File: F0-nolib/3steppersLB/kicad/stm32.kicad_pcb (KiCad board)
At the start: 2 copper layers, 97 x 69.5 mm, 103 parts, among them J1 01x03, J10 Screw_Terminal_01x03, J11 USB_B, J12 Screw_Terminal_01x02, J13 Screw_Terminal_01x02, J14 Conn_01x04_Female, J15 Conn_01x04_Female, J16 Conn_01x04_Female, J17 Conn_01x04_Female, J18 buzzer, J2 Conn_01x04_Female, J3 Conn_01x04_Female, J4 Conn_01x04_Female, J5 Conn_01x04_Female, J6 01x03, J7 Screw_Terminal_01x03, J8 01x05, J9 01x05, K1 G5LE-1, P1 Hole, P2 Hole, P6 Hole, P7 Hole, Q1 B0505S, Q2 SI2300, Q3 SI2300, Q4 SI2300, Q5 IRF9310, SW1 SW_DIP_x01, U1 ISO1050DUB, U2 STM32F072C8Tx, U3 LM2576-5.0, U4 CD4050, U5 CD4050, U6 LM1117-3.3

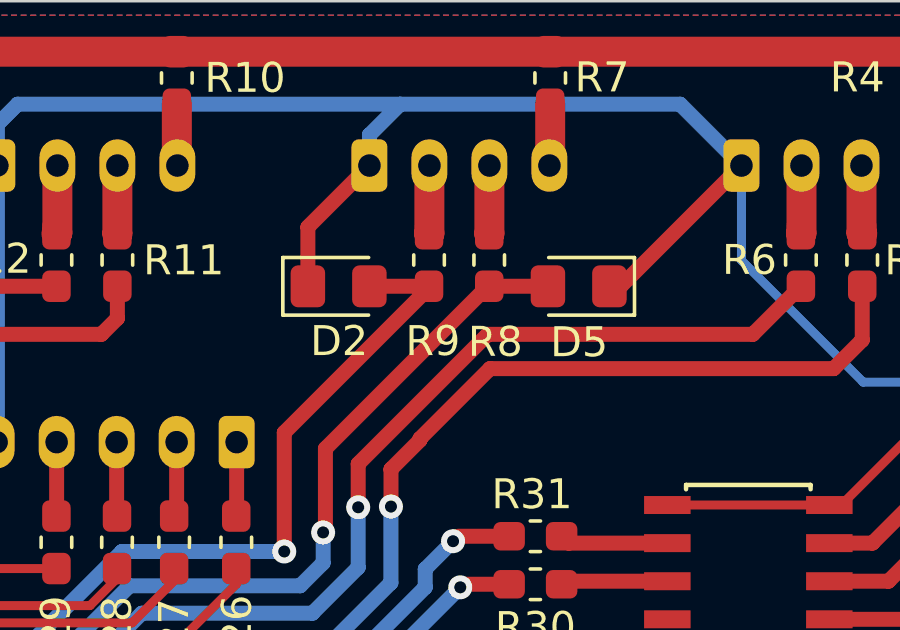
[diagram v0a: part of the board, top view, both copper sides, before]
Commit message: fixed some bugs in 3steppersLB schematic
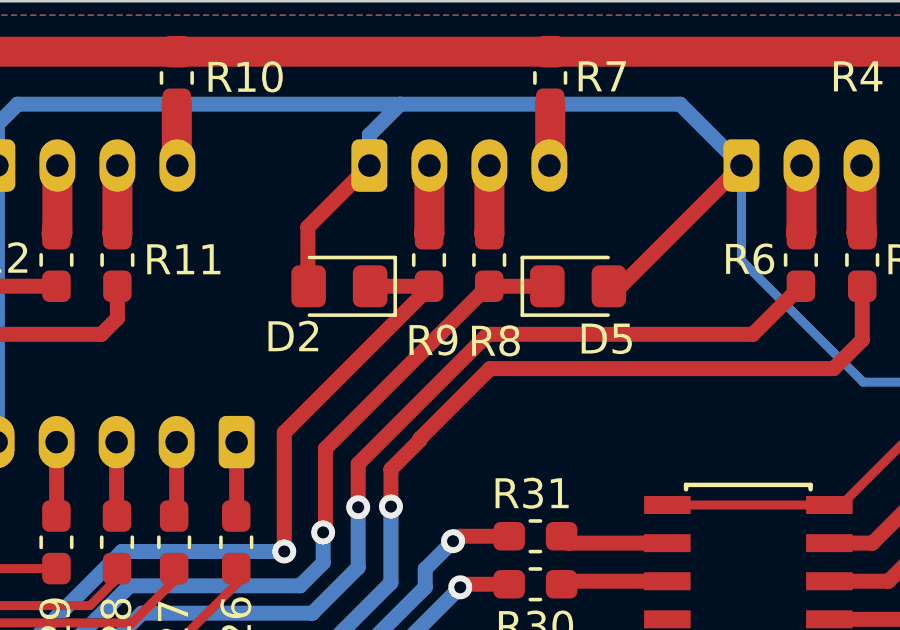
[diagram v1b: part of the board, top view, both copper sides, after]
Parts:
- D2, D5: value D -> CESD3V3
- turned D2 to 180 degrees
- turned D5 to 0 degrees
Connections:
- D2 pad 1: GND -> /Enc2b
- D2 pad 2: /Enc2b -> GND
- D5 pad 1: GND -> /Enc2a
- D5 pad 2: /Enc2a -> GND
- Q4 pad 2: Net-(Q4-Pad2) -> GND
- R33 pad 2: Net-(Q4-Pad2) -> GND
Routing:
- net GND: track 546.0 -> 548.1 mm
- net Net-(Q4-Pad2): track 2.12 -> 0.00 mm
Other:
- board text added: "CAN terminator"
- board text added: "ON"
